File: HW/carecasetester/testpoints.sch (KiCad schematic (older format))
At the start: 15 parts, among them J15 Conn_01x16_Male, J15-TP1 Conn_01x01_Male, J16-TP2 Conn_01x01_Male, J17-TP3 Conn_01x01_Male, J18-TP4 Conn_01x01_Male, J19-TP6 Conn_01x01_Male, J20-TP9 Conn_01x01_Male, J21-TP10 Conn_01x01_Male, J22-TP11 Conn_01x01_Male, J23-TP12 Conn_01x01_Male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

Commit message: cc-tester v0.1 gerber filser genereret og 1. print bestilles
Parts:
- removed J28-TP27: Conn_01x01_Male, MM:P50-E-120-G(Pogo)_0.7mmHole_1.5mmPad, symbol Connector:Conn_01x01_Male
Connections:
- net GND: now also J15.15 (Pin_15)
- net TP4: now reaches J15.4 (Pin_4), J17-TP3.1 (Pin_1)
- net TP5: now reaches J15.12 (Pin_12), J25-TP18.1 (Pin_1)
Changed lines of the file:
@@
 $Descr A4 11693 8268
 encoding utf-8
-Sheet 4 5
+Sheet 4 6
 Title ""
 Date ""
@@
 $EndComp
 $Comp
-L Connector:Conn_01x01_Male J25-TP?
-U 1 1 5E3E0E0E
-P 8650 3675
-AR Path="/5E3BA6A3/5E3E0E0E" Ref="J25-TP?"  Part="1"
-AR Path="/5E3DBE35/5E3E0E0E" Ref="J28-TP27"  Part="1"
-F 0 "J28-TP27" H 8622 3607 50  0000 R CNN
-F 1 "Conn_01x01_Male" H 8622 3698 50  0000 R CNN
-F 2 "MM:P50-E-120-G(Pogo)_0.7mmHole_1.5mmPad" H 8650 3675 50  0001 C CNN
-F 3 "~" H 8650 3675 50  0001 C CNN
-	1    8650 3675
-	-1   0    0    1
-$EndComp
-$Comp
 L Connector:Conn_01x16_Male J15
 U 1 1 5E3E19EF
@@
 	8450 1925 8450 1875
 Wire Wire Line
-	8450 2025 5900 2025
-Wire Wire Line
 	5900 2125 8450 2125
 Wire Wire Line
@@
 	7775 3075 8450 3075
 Wire Wire Line
-	5900 2825 7650 2825
-Wire Wire Line
 	7650 2825 7650 3225
 Wire Wire Line
@@
 Wire Wire Line
 	7400 3525 8450 3525
-Wire Wire Line
-	5900 3125 7275 3125
-Wire Wire Line
-	7275 3125 7275 3675
-Wire Wire Line
-	7275 3675 8450 3675
 $Comp
 L power:GND #PWR05
@@
 	5900 1725 6000 1725
 Wire Wire Line
-	6000 1725 6000 3225
+	6000 1725 6000 3125
 Connection ~ 6000 3225
+Wire Wire Line
+	5900 3125 6000 3125
+Connection ~ 6000 3125
+Wire Wire Line
+	6000 3125 6000 3225
+Text HLabel 6350 4050 0    50   Input ~ 0
+TP4
+Text HLabel 6750 4250 0    50   Input ~ 0
+TP5
+Wire Wire Line
+	6750 4250 6750 2825
+Wire Wire Line
+	5900 2825 6750 2825
+Connection ~ 6750 2825
+Wire Wire Line
+	6750 2825 7650 2825
+Wire Wire Line
+	6350 4050 6350 2025
+Wire Wire Line
+	5900 2025 6350 2025
+Connection ~ 6350 2025
+Wire Wire Line
+	6350 2025 8450 2025
 $EndSCHEMATC

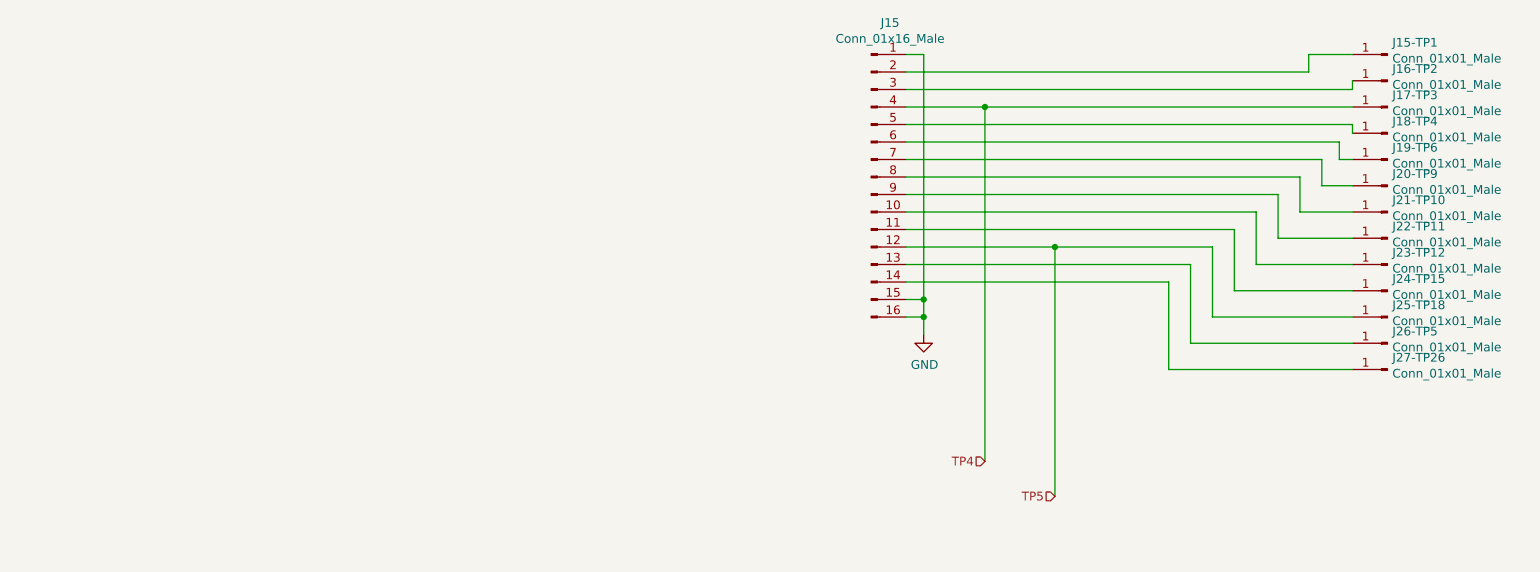
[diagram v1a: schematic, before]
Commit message: working speaker outputs set with pull down (internal arduino)
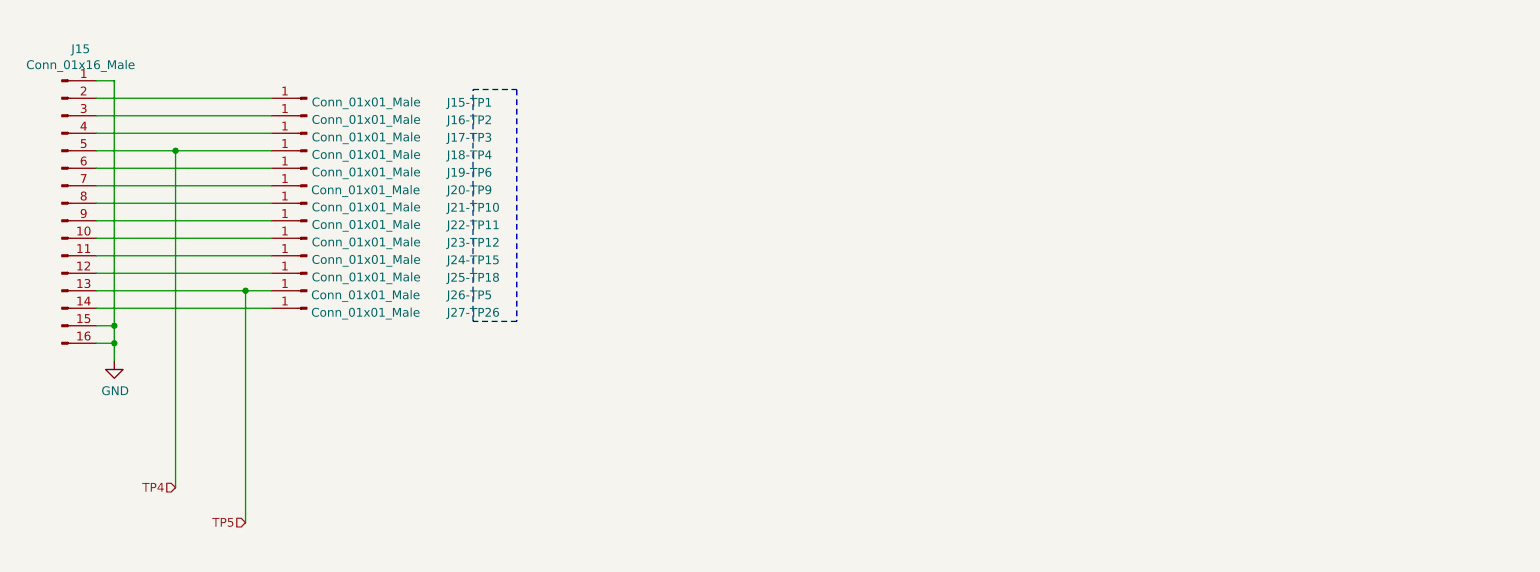
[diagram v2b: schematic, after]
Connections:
- net TP4: now also J15.5 (Pin_5), J18-TP4.1 (Pin_1); no longer J15.4 (Pin_4), J17-TP3.1 (Pin_1)
- net TP5: now also J15.13 (Pin_13), J26-TP5.1 (Pin_1); no longer J15.12 (Pin_12), J25-TP18.1 (Pin_1)
- new net: J15.4 (Pin_4), J17-TP3.1 (Pin_1)
- new net: J15.12 (Pin_12), J25-TP18.1 (Pin_1)
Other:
- moved on the sheet: J15, J15-TP1, J16-TP2, J17-TP3, J18-TP4, J19-TP6, J20-TP9, J21-TP10, J22-TP11, J23-TP12, J24-TP15, J25-TP18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

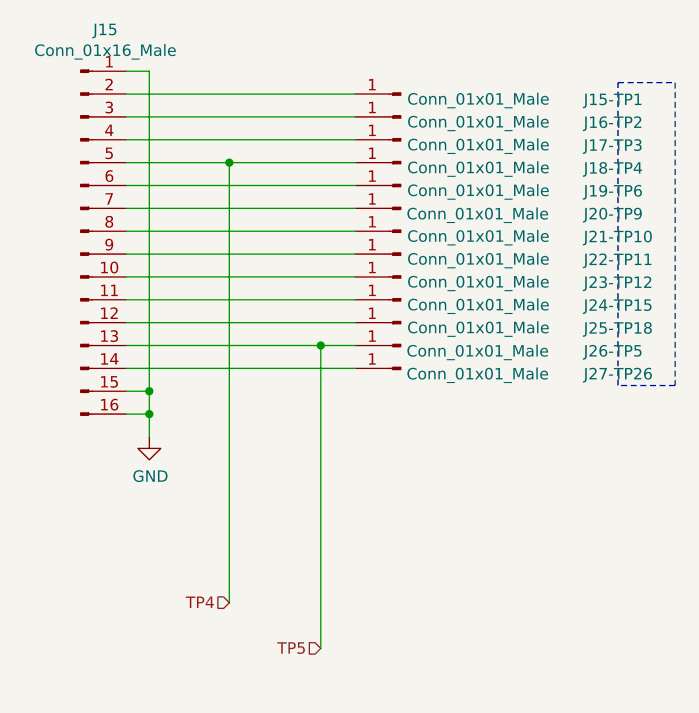
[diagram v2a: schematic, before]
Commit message: CC tester : tp25 added tp8 moved tp20 moved
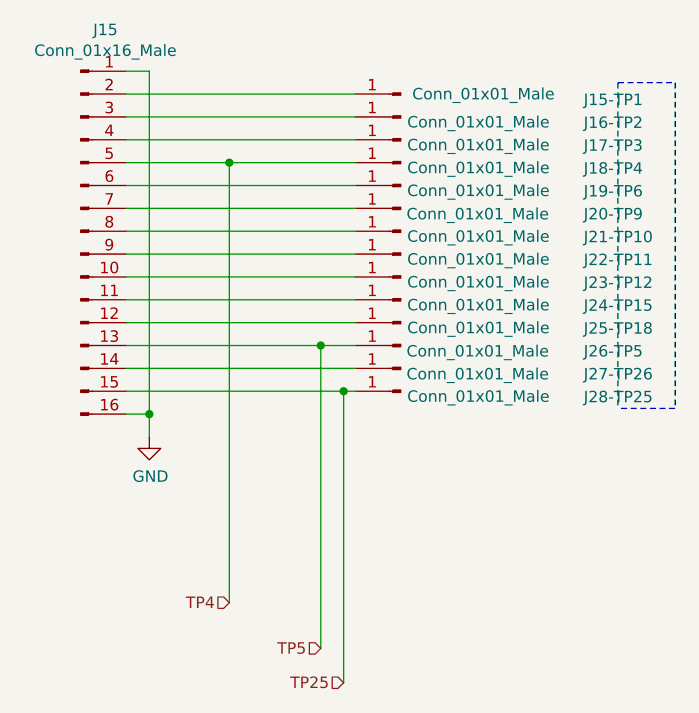
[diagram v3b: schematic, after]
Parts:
- added J28-TP25: Conn_01x01_Male, MM:P50-E-120-G(Pogo)_0.7mmHole_1.5mmPad, symbol Connector:Conn_01x01_Male
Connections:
- net GND: no longer J15.15 (Pin_15)
- new net TP25: J15.15 (Pin_15), J28-TP25.1 (Pin_1)
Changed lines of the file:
@@
 AR Path="/5E3DBE35/5E3DEA4C" Ref="J15-TP1"  Part="1"
 F 0 "J15-TP1" H 1675 2000 50  0000 R CNN
-F 1 "Conn_01x01_Male" H 2447 1998 50  0000 R CNN
+F 1 "Conn_01x01_Male" H 2425 1975 50  0000 R CNN
 F 2 "MM:P50-E-120-G(Pogo)_0.7mmHole_1.5mmPad" H 2475 1975 50  0001 C CNN
 F 3 "~" H 2475 1975 50  0001 C CNN
@@
 Wire Wire Line
 	1275 1875 1375 1875
-Wire Wire Line
-	1375 1875 1375 3275
 Connection ~ 1375 3375
-Wire Wire Line
-	1275 3275 1375 3275
-Connection ~ 1375 3275
-Wire Wire Line
-	1375 3275 1375 3375
 Text HLabel 1725 4200 0    50   Input ~ 0
 TP4
@@
 	1275 3175 2275 3175
 Wire Notes Line
-	3675 1925 3675 3250
-Wire Notes Line
-	3675 3250 3425 3250
-Wire Notes Line
-	3425 3250 3425 1925
+	3675 3350 3425 3350
 Wire Notes Line
 	3425 1925 3675 1925
@@
 Wire Wire Line
 	1725 2275 2275 2275
+Wire Wire Line
+	1375 1875 1375 3375
+$Comp
+L Connector:Conn_01x01_Male J?
+U 1 1 5F295961
+P 2475 3275
+AR Path="/5E3BA6A3/5F295961" Ref="J?"  Part="1"
+AR Path="/5E3DBE35/5F295961" Ref="J28-TP25"  Part="1"
+F 0 "J28-TP25" H 1675 3300 50  0000 R CNN
+F 1 "Conn_01x01_Male" H 2447 3298 50  0000 R CNN
+F 2 "MM:P50-E-120-G(Pogo)_0.7mmHole_1.5mmPad" H 2475 3275 50  0001 C CNN
+F 3 "~" H 2475 3275 50  0001 C CNN
+	1    2475 3275
+	-1   0    0    1
+$EndComp
+Wire Notes Line
+	3425 1925 3425 3350
+Wire Notes Line
+	3675 1925 3675 3350
+Wire Wire Line
+	1275 3275 2225 3275
+Text HLabel 2225 4550 0    50   Input ~ 0
+TP25
+Wire Wire Line
+	2225 4550 2225 3275
+Connection ~ 2225 3275
+Wire Wire Line
+	2225 3275 2275 3275
 $EndSCHEMATC
